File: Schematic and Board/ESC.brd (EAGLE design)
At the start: 47.6 x 29.8 mm, 45 parts

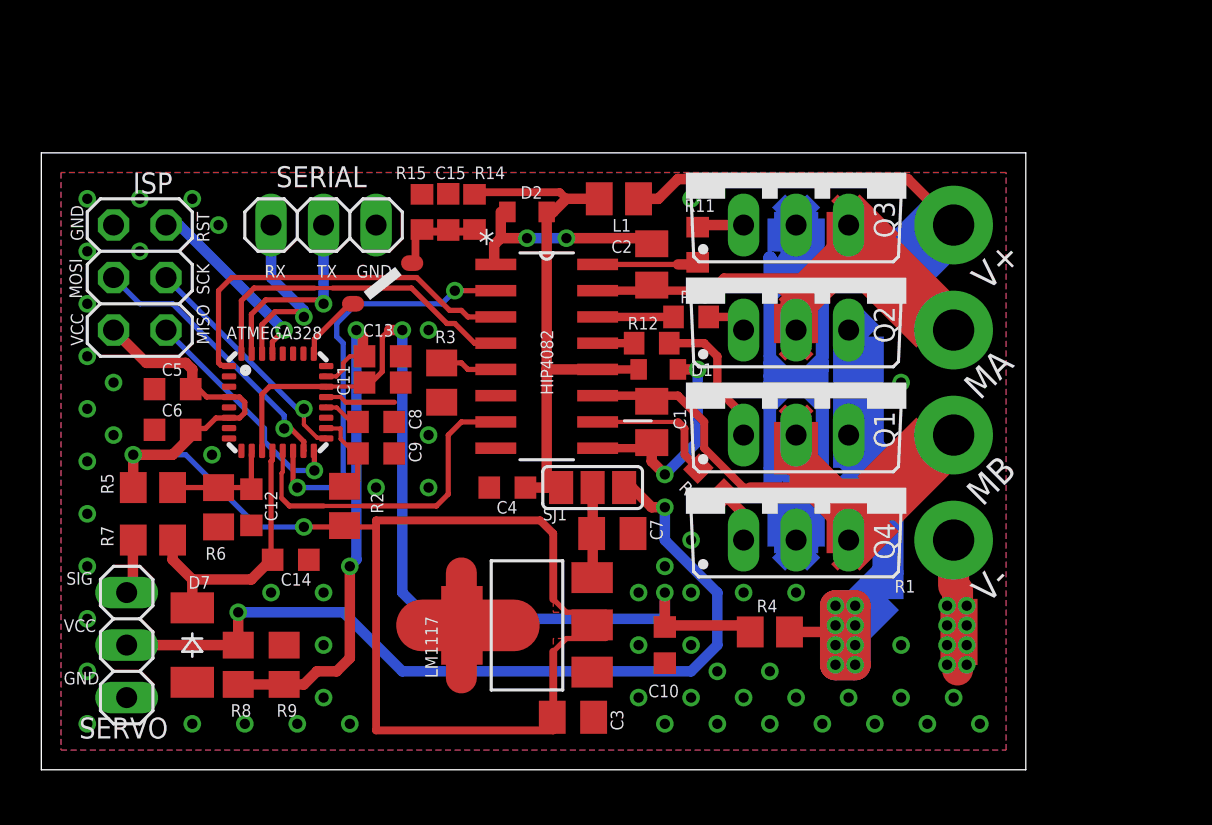
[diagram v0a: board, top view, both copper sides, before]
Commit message: updated board: makes better use of PWM outputs, also adds optional ACS712 hall effect current sensor
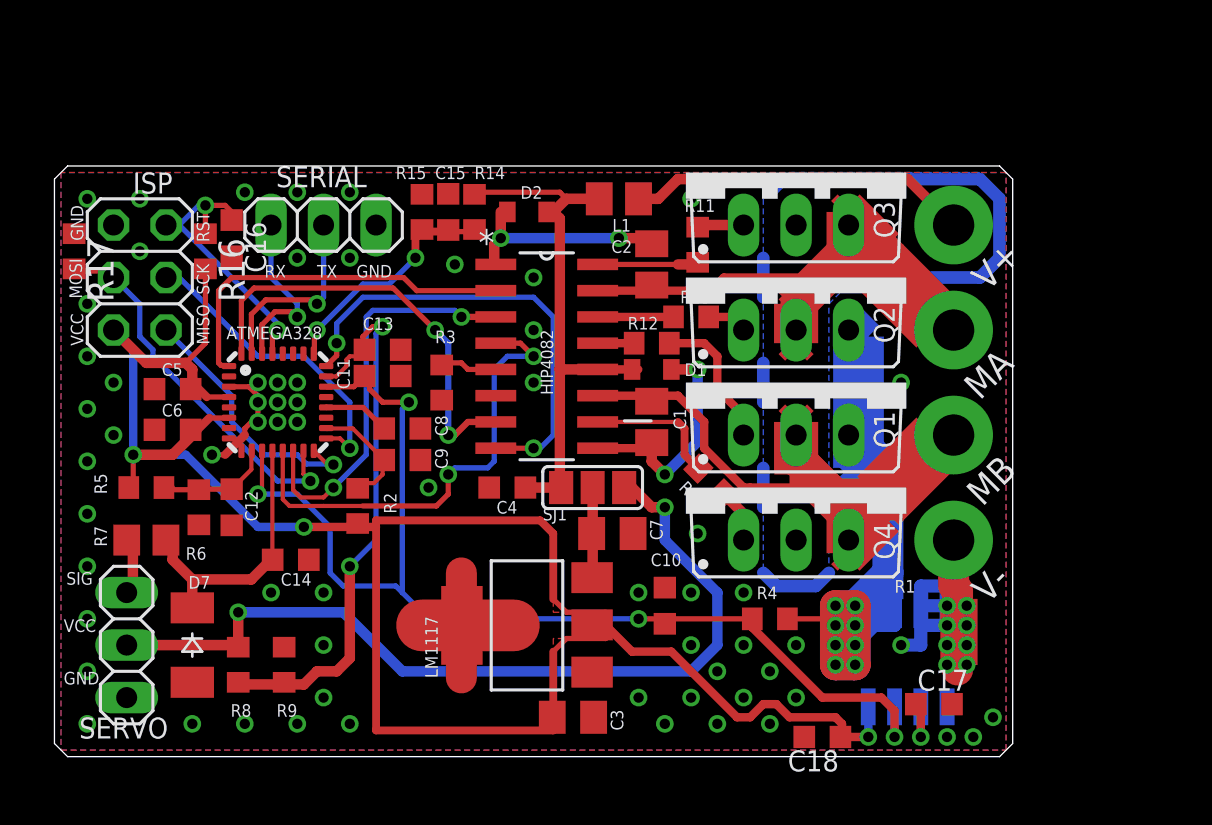
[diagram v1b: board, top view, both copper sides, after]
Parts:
- added C16, C17, C18: 100nF, rcl:C0603K
- added IC1: ACS712, ACS712:SO08
- added R16, R17: 1k, rcl:R0603
- R2, R3, R4, R8, R9: device rcl:R0805 -> rcl:R0603
- R5: value 5k6 -> 33k; device rcl:R0805 -> rcl:R0603
- R6: value 1k -> 10k; device rcl:R0805 -> rcl:R0603
- moved C10 1.91 mm to (29.2, 6.99), turned to 90 degrees
- moved C8 1.31 mm to (16.5, 15.6)
- moved C9 1.31 mm to (16.5, 14.0)
- moved R6 0.95 mm to (6.67, 11.7)
- moved C12 0.95 mm to (8.26, 11.7)
- moved R2 0.64 mm to (14.4, 11.8)
- moved R4 0.63 mm to (34.3, 6.35)
- moved R5 0.32 mm to (4.13, 12.7)
- moved R7 0.32 mm to (4.13, 10.2)
- moved C11 0.32 mm to (15.6, 18.1)
- moved C13 0.32 mm to (15.6, 19.4)
- moved D1 0.32 mm to (28.6, 18.4)
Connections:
- new net AHI: ATMEGA328.32, HIP4082.7
- new net BHI: ATMEGA328.1, HIP4082.2
- net +5V: now also C18.1, IC1.8, R16.2
- net GND: now also ATMEGA328.2, ATMEGA328.7, ATMEGA328.8, ATMEGA328.9, C16.2, C17.2, C18.2, IC1.3, IC1.4, IC1.5, R17.1; no longer HIP4082.8
- net I_SENSE: now also IC1.7
- net MOSI: now also R17.2
- net N$14: now also ATMEGA328.24, HIP4082.8; no longer ATMEGA328.32, HIP4082.4
- net N$15: now also C17.1, IC1.6; no longer ATMEGA328.1, HIP4082.3
- net OC1A: now also HIP4082.4; no longer HIP4082.7
- net OC1B: now also HIP4082.3; no longer HIP4082.2
- net RESET: now also C16.1, R16.1
- net SENSE: now also IC1.1, IC1.2
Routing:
- net +12V: track 121.9 -> 48.4 mm
- net +5V: track 81.8 -> 108.9 mm, vias 2 -> 3
- net AHI: track 0.00 -> 20.9 mm, vias 0 -> 2
- net BHI: track 0.00 -> 18.0 mm
- net N$15: track 18.5 -> 3.29 mm, vias 0 -> 1
- net I_SENSE: track 45.1 -> 56.2 mm, vias 2 -> 4
- net GND: track 9.79 -> 20.7 mm, vias 66 -> 73
- net OC1A: track 16.2 -> 22.9 mm, vias 0 -> 2
- net N$14: track 16.2 -> 22.4 mm, vias 0 -> 2
- net MOSI: track 13.3 -> 18.4 mm
- net SENSE: track 56.3 -> 60.9 mm
- net RESET: track 9.22 -> 13.8 mm, vias 1 -> 2
- net VSENSE: track 8.14 -> 11.7 mm, vias 0 -> 2
- net SCK: track 11.5 -> 14.9 mm
- net N$19: track 26.1 -> 27.7 mm
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- added copper zone on layer 16, net +12V
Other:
- board size 47.6 x 29.8 mm -> 46.4 x 28.6 mm

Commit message: 24V adaption - add 7812, expand board, add VMM capacitors, add encoder input.
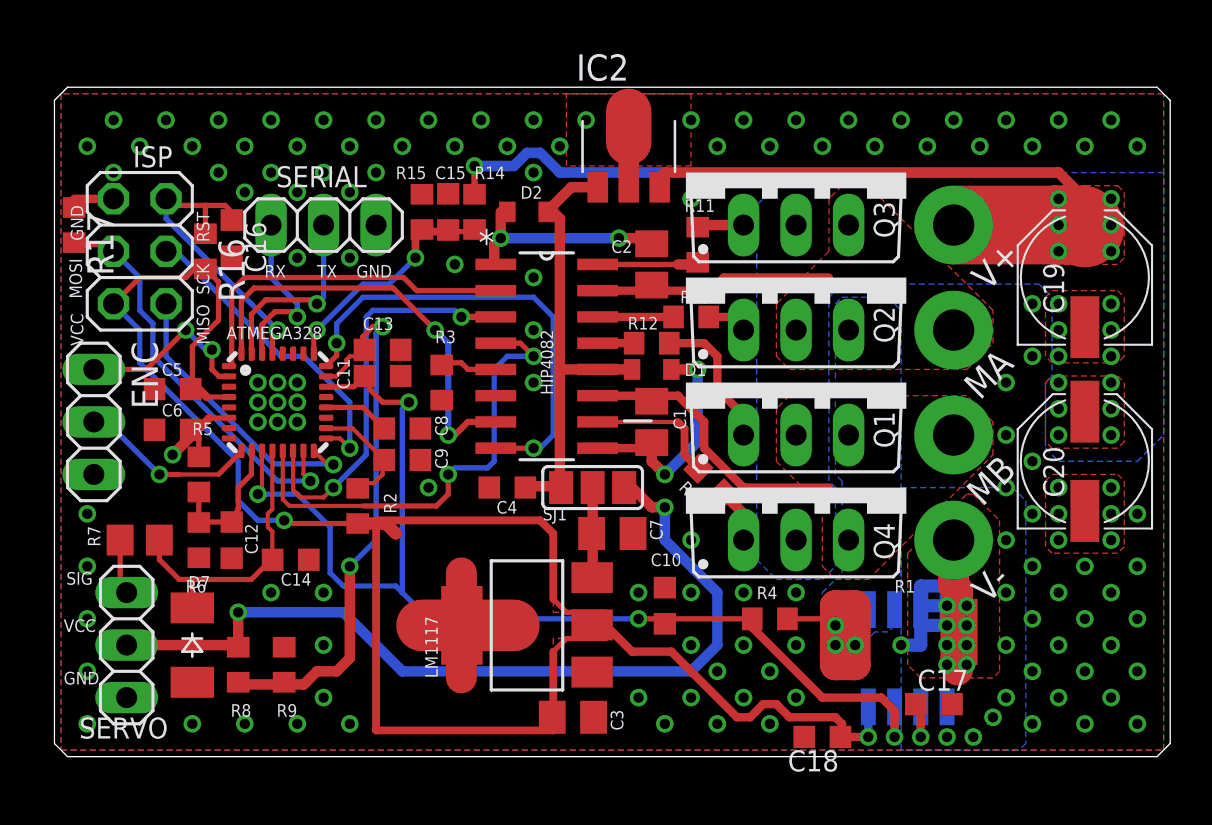
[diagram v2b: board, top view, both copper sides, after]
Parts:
- removed L1: L, rcl:M0805
- added C19, C20: 100uF, rcl:PANASONIC_D
- added ENC: ENC, pinhead:1X03
- added IC2: 78L12F, linear:SOT89
- R14: value 22k -> 33k
- moved R5 2.62 mm to (6.67, 13.3), turned to 90 degrees
- moved C12 1.59 mm to (8.26, 10.2)
- moved R6 1.59 mm to (6.67, 10.2)
- moved ISP 1.27 mm to (3.81, 24.1)
- moved R17 1.27 mm to (0.64, 25.4)
- moved R7 0.32 mm to (3.81, 10.2)
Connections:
- net N$14 renamed DISABLE
- net N$4 renamed SERVO_IN
- new net N$19: ATMEGA328.2, ENC.1
- new net N$22: ATMEGA328.9, ENC.2
- net +12V: now also C4.1, D1.A, D2.A, HIP4082.12, IC2.1, SJ1.1; no longer L1.2, Q3.D, Q4.D
- net GND: now also C19.-, C20.-, ENC.3, IC2.2, IC2.2@1; no longer ATMEGA328.2, ATMEGA328.7, ATMEGA328.8, ATMEGA328.9
- net VCC: now also C19.+, C20.+, IC2.3, Q3.D, Q4.D; no longer C4.1, D1.A, D2.A, HIP4082.12, L1.1, SJ1.1
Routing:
- net MO_B: track 57.9 -> 11.8 mm
- net MO_A: track 60.1 -> 14.1 mm
- net SENSE: track 60.9 -> 15.5 mm, vias 8 -> 3
- net VCC: track 26.9 -> 64.2 mm, vias 0 -> 14
- net +12V: track 48.4 -> 22.0 mm, vias 1 -> 0
- net N$19: track 0.00 -> 8.82 mm, vias 0 -> 2
- net N$22: track 0.00 -> 8.69 mm, vias 0 -> 1
- net +5V: track 108.9 -> 110.2 mm
- net RESET: track 13.8 -> 15.1 mm, vias 2 -> 1
- net MOSI: track 18.4 -> 19.7 mm
- net MISO: track 12.8 -> 14.0 mm
- net GND: track 20.7 -> 19.6 mm, vias 73 -> 149
- net BHI: track 18.0 -> 17.0 mm
- net N$12: track 5.99 -> 6.85 mm
- net SCK: track 14.9 -> 15.5 mm
- added copper zone on layer 1, net MO_A
- added copper zone on layer 1, net MO_B
- added copper zone on layer 16, net SENSE
- added copper zone on layer 1, net VCC
- added copper zone on layer 16, net VCC
- removed copper zone on layer 16, net +12V
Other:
- board size 46.4 x 28.6 mm -> 54 x 32.4 mm

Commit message: Minor tidying
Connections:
- net N$23 renamed SERVO_VSENSE
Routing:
- net OC1A: track 22.9 -> 21.1 mm
- net SERVO_VSENSE: track 27.7 -> 26.9 mm

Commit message: More board tweaks
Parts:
- added C21: 100nF, rcl:C0603K
- Q1, Q2, Q3, Q4: value (none) -> IRL1404Z
- R1: value 0R05 -> 0R005
- moved R4 1.27 mm to (33.0, 6.35)
- moved R16 0.64 mm to (6.99, 24.8)
- moved R7 0.32 mm to (3.49, 10.2)
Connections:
- net +12V: now also C21.1
- net GND: now also C21.2
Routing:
- net N$19: track 8.82 -> 23.7 mm
- net RESET: track 15.0 -> 29.9 mm
- net GND: track 19.5 -> 25.7 mm, vias 149 -> 148
- net SENSE: track 15.5 -> 21.6 mm, vias 3 -> 12
- net N$17: track 42.1 -> 36.9 mm
- net SCK: track 15.5 -> 18.2 mm
- net +5V: track 109.9 -> 108.5 mm
- net +12V: track 22.0 -> 23.2 mm
- net MISO: track 14.2 -> 15.0 mm
- net MOSI: track 19.9 -> 20.4 mm
- net BHI: track 17.0 -> 16.4 mm

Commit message: Remove ACS712, improve ground stitching and layout
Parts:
- removed C17, C18: 100nF, rcl:C0603K
- removed IC1: ACS712, ACS712:SO08
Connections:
- removed net N$15: C17.1, IC1.6
- net +5V: no longer C18.1, IC1.8
- net GND: no longer C17.2, C18.2, IC1.3, IC1.4, IC1.5
- net I_SENSE: no longer IC1.7
- net SENSE: no longer IC1.1, IC1.2
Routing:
- net +5V: track 108.5 -> 49.6 mm, vias 3 -> 2
- net I_SENSE: track 56.7 -> 43.4 mm, vias 4 -> 3
- net GND: track 25.7 -> 18.1 mm, vias 148 -> 151
- net N$15: track 3.29 -> 0.00 mm, vias 1 -> 0
- net SENSE: track 21.6 -> 21.1 mm
